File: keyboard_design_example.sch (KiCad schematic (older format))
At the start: 24 parts, among them SW1 SW_PUSH, U1 ATmega32U4-AU, Y1 16MHz

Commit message: Update and work
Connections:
- net +5V: no longer C1.2, C2.2, C3.2, C4.2, C5.2, C6.2, C7.2, R4.1, SW1.1, U1.15 (GND), U1.23 (GND), U1.35 (GND), U1.43 (GND), U1.5 (UGND), USB1.1 (GND), Y1.2, Y1.4
- new net GND: C1.2, C2.2, C3.2, C4.2, C5.2, C6.2, C7.2, R4.1, SW1.1, U1.15 (GND), U1.23 (GND), U1.35 (GND), U1.43 (GND), U1.5 (UGND), USB1.1 (GND), Y1.2, Y1.4
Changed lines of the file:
@@
 Wire Wire Line
 	5750 2100 5650 2100
-$Comp
-L keyboard_parts:GND #PWR0102
-U 1 1 60214B8A
-P 5400 5800
-F 0 "#PWR0102" H 5400 5850 20  0001 C CNN
-F 1 "GND" H 5400 5859 30  0000 C CNN
-F 2 "" H 5400 5800 60  0000 C CNN
-F 3 "" H 5400 5800 60  0000 C CNN
-	1    5400 5800
-	1    0    0    -1
-$EndComp
 Wire Wire Line
 	5750 5700 5650 5700
@@
 	0    1    1    0
 $EndComp
-$Comp
-L keyboard_parts:GND #PWR0103
-U 1 1 602192CF
-P 7500 4500
-F 0 "#PWR0103" H 7500 4550 20  0001 C CNN
-F 1 "GND" H 7500 4559 30  0000 C CNN
-F 2 "" H 7500 4500 60  0000 C CNN
-F 3 "" H 7500 4500 60  0000 C CNN
-	1    7500 4500
-	1    0    0    -1
-$EndComp
 Wire Wire Line
 	6350 4500 6900 4500
@@
 Wire Wire Line
 	4750 3700 4750 3850
-$Comp
-L keyboard_parts:GND #PWR0104
-U 1 1 6022339F
-P 4750 4250
-F 0 "#PWR0104" H 4750 4300 20  0001 C CNN
-F 1 "GND" H 4750 4309 30  0000 C CNN
-F 2 "" H 4750 4250 60  0000 C CNN
-F 3 "" H 4750 4250 60  0000 C CNN
-	1    4750 4250
-	1    0    0    -1
-$EndComp
 Wire Wire Line
 	4750 4050 4750 4250
@@
 Wire Wire Line
 	4250 3000 4100 3000
-$Comp
-L keyboard_parts:GND #PWR0106
-U 1 1 60232D3A
-P 4100 3100
-F 0 "#PWR0106" H 4100 3150 20  0001 C CNN
-F 1 "GND" H 4100 3159 30  0000 C CNN
-F 2 "" H 4100 3100 60  0000 C CNN
-F 3 "" H 4100 3100 60  0000 C CNN
-	1    4100 3100
-	1    0    0    -1
-$EndComp
 Wire Wire Line
 	4100 3000 4100 3100
@@
 Wire Wire Line
 	5150 2400 5100 2400
-$Comp
-L keyboard_parts:GND #PWR0107
-U 1 1 6023828E
-P 4400 2100
-F 0 "#PWR0107" H 4400 2150 20  0001 C CNN
-F 1 "GND" H 4400 2159 30  0000 C CNN
-F 2 "" H 4400 2100 60  0000 C CNN
-F 3 "" H 4400 2100 60  0000 C CNN
-	1    4400 2100
-	1    0    0    -1
-$EndComp
 $Comp
 L power:+5V #PWR0108
@@
 F 3 "" H 3600 4550 50  0001 C CNN
 	1    3600 4550
-	1    0    0    -1
-$EndComp
-$Comp
-L keyboard_parts:GND #PWR0110
-U 1 1 60244FF0
-P 3600 4950
-F 0 "#PWR0110" H 3600 5000 20  0001 C CNN
-F 1 "GND" H 3600 5009 30  0000 C CNN
-F 2 "" H 3600 4950 60  0000 C CNN
-F 3 "" H 3600 4950 60  0000 C CNN
-	1    3600 4950
 	1    0    0    -1
 $EndComp
@@
 Wire Wire Line
 	8450 2100 8450 2150
-$Comp
-L keyboard_parts:GND #PWR0113
-U 1 1 602538F7
-P 8450 2150
-F 0 "#PWR0113" H 8450 2200 20  0001 C CNN
-F 1 "GND" H 8450 2209 30  0000 C CNN
-F 2 "" H 8450 2150 60  0000 C CNN
-F 3 "" H 8450 2150 60  0000 C CNN
-	1    8450 2150
-	1    0    0    -1
-$EndComp
 Wire Wire Line
 	8300 1900 8500 1900
@@
 Wire Wire Line
 	4450 2100 4400 2100
+$Comp
+L power:GND #PWR0102
+U 1 1 60242F11
+P 3600 4950
+F 0 "#PWR0102" H 3600 4700 50  0001 C CNN
+F 1 "GND" H 3605 4777 50  0000 C CNN
+F 2 "" H 3600 4950 50  0001 C CNN
+F 3 "" H 3600 4950 50  0001 C CNN
+	1    3600 4950
+	1    0    0    -1
+$EndComp
+$Comp
+L power:GND #PWR0103
+U 1 1 60247D6C
+P 4100 3100
+F 0 "#PWR0103" H 4100 2850 50  0001 C CNN
+F 1 "GND" H 4105 2927 50  0000 C CNN
+F 2 "" H 4100 3100 50  0001 C CNN
+F 3 "" H 4100 3100 50  0001 C CNN
+	1    4100 3100
+	1    0    0    -1
+$EndComp
+$Comp
+L power:GND #PWR0104
+U 1 1 60249D69
+P 4400 2100
+F 0 "#PWR0104" H 4400 1850 50  0001 C CNN
+F 1 "GND" H 4405 1927 50  0000 C CNN
+F 2 "" H 4400 2100 50  0001 C CNN
+F 3 "" H 4400 2100 50  0001 C CNN
+	1    4400 2100
+	1    0    0    -1
+$EndComp
+$Comp
+L power:GND #PWR0106
+U 1 1 6024BCD7
+P 7500 4500
+F 0 "#PWR0106" H 7500 4250 50  0001 C CNN
+F 1 "GND" H 7505 4327 50  0000 C CNN
+F 2 "" H 7500 4500 50  0001 C CNN
+F 3 "" H 7500 4500 50  0001 C CNN
+	1    7500 4500
+	1    0    0    -1
+$EndComp
+$Comp
+L power:GND #PWR0107
+U 1 1 6024DB1C
+P 5400 5800
+F 0 "#PWR0107" H 5400 5550 50  0001 C CNN
+F 1 "GND" H 5405 5627 50  0000 C CNN
+F 2 "" H 5400 5800 50  0001 C CNN
+F 3 "" H 5400 5800 50  0001 C CNN
+	1    5400 5800
+	1    0    0    -1
+$EndComp
+$Comp
+L power:GND #PWR0110
+U 1 1 6024FA6D
+P 4750 4250
+F 0 "#PWR0110" H 4750 4000 50  0001 C CNN
+F 1 "GND" H 4755 4077 50  0000 C CNN
+F 2 "" H 4750 4250 50  0001 C CNN
+F 3 "" H 4750 4250 50  0001 C CNN
+	1    4750 4250
+	1    0    0    -1
+$EndComp
+$Comp
+L power:GND #PWR0113
+U 1 1 60251816
+P 8450 2150
+F 0 "#PWR0113" H 8450 1900 50  0001 C CNN
+F 1 "GND" H 8455 1977 50  0000 C CNN
+F 2 "" H 8450 2150 50  0001 C CNN
+F 3 "" H 8450 2150 50  0001 C CNN
+	1    8450 2150
+	1    0    0    -1
+$EndComp
 $EndSCHEMATC

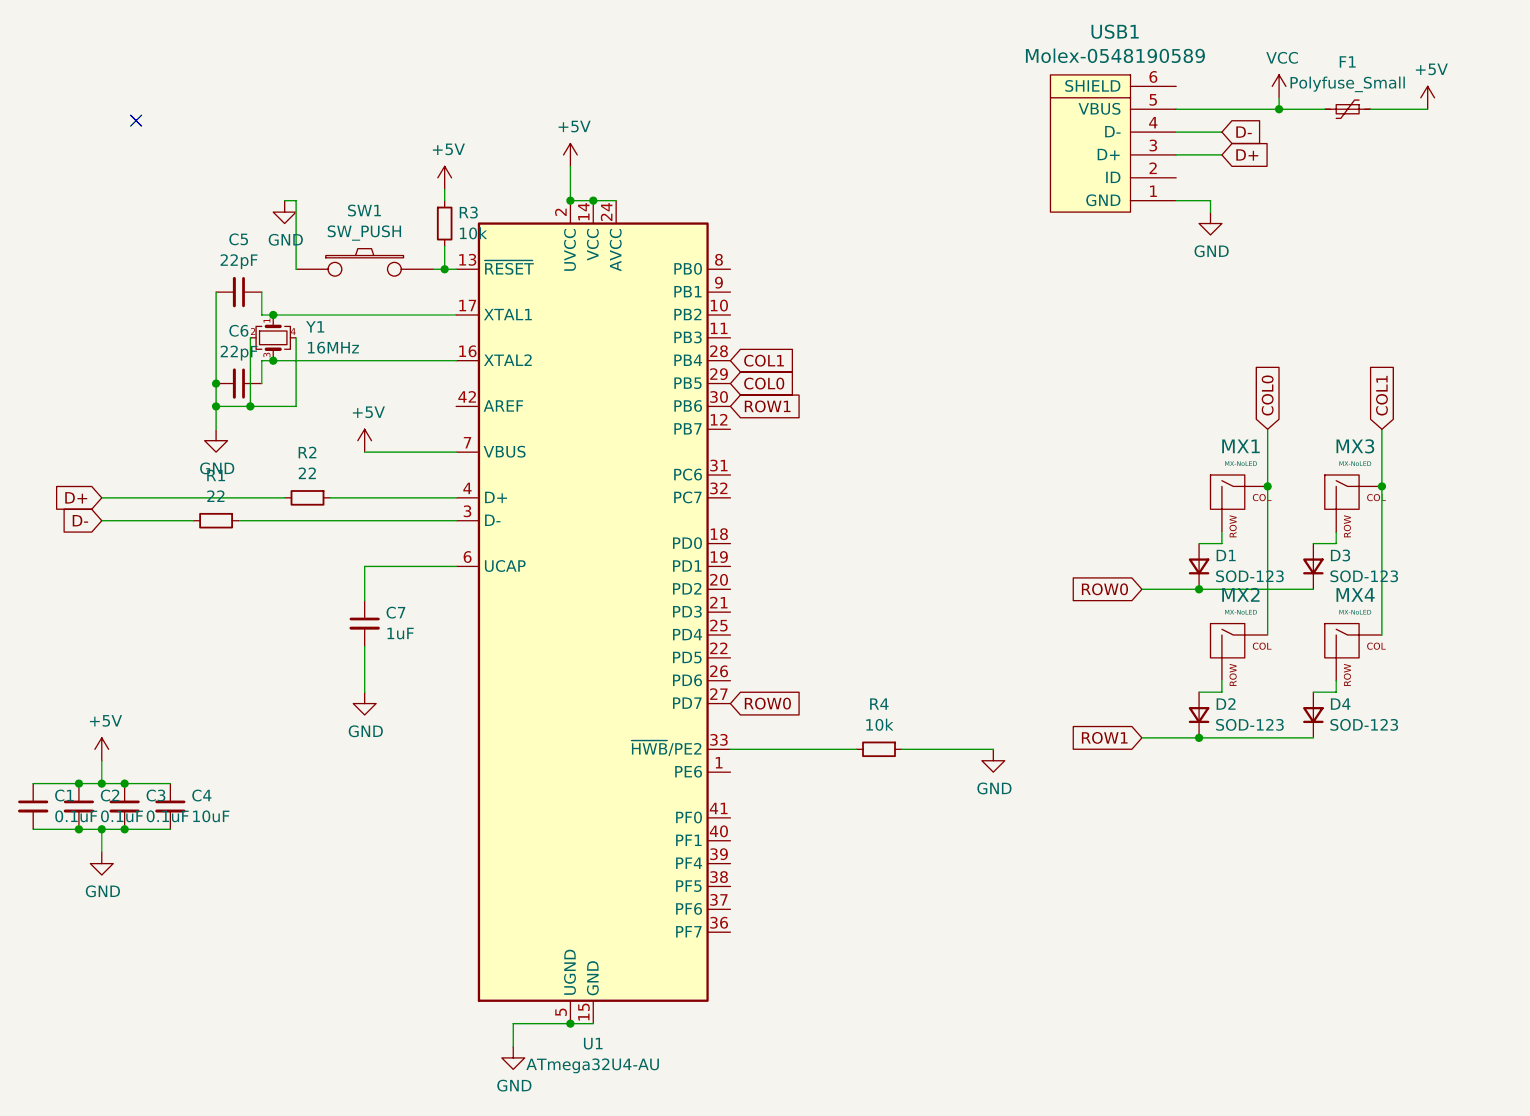
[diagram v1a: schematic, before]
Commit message: 2x2 bad 3x3 good
Updated schematic for a 3x3 mx switch cluster.
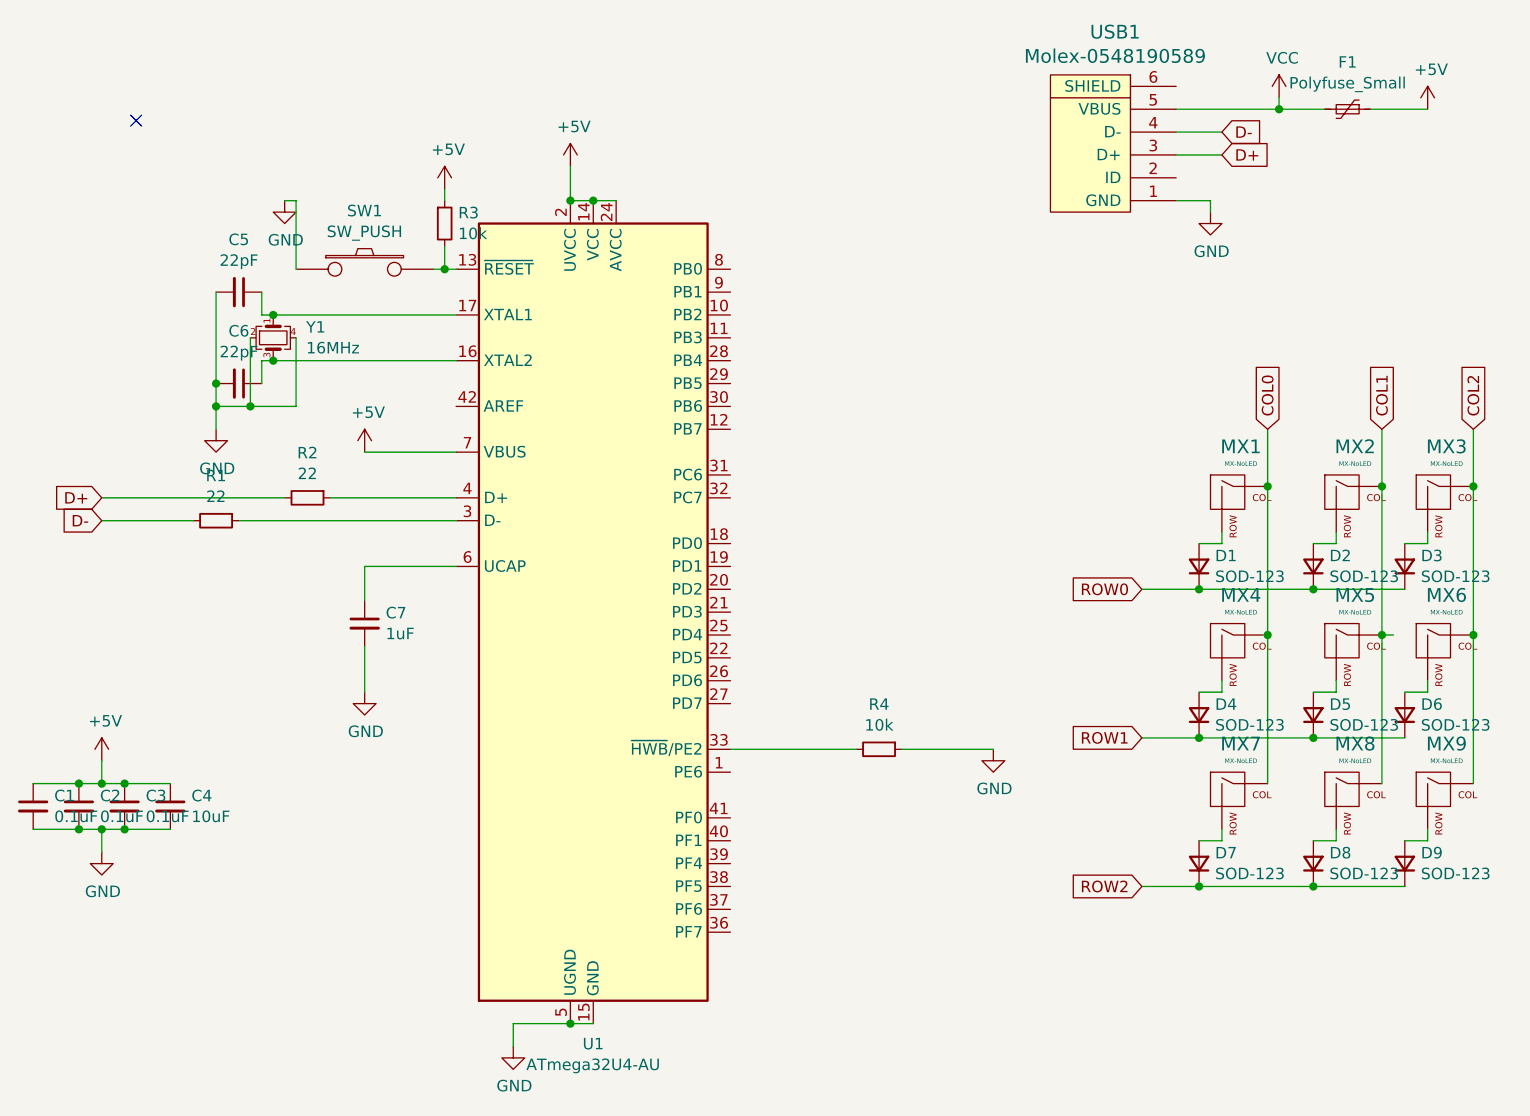
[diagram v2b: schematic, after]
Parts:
- added D3, D6, D7, D8, D9: SOD-123, symbol Device:D_Small
- added MX3, MX6, MX7, MX8, MX9: MX-NoLED, symbol MX_Alps_Hybrid:MX-NoLED
- renumbered D3 to D2, D2 to D4, D4 to D5, MX3 to MX2, MX2 to MX4, MX4 to MX5
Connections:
- net COL0: now also MX7.1 (COL); no longer U1.29 (PB5)
- net COL1: now also MX8.1 (COL); no longer U1.28 (PB4)
- net ROW0: now also D3.1 (K); no longer U1.27 (PD7)
- net ROW1: now also D6.1 (K); no longer U1.30 (PB6)
- new net: D3.2 (A), MX3.2 (ROW)
- new net: D6.2 (A), MX6.2 (ROW)
- new net: D8.2 (A), MX8.2 (ROW)
- new net: D9.2 (A), MX9.2 (ROW)
- new net: D7.2 (A), MX7.2 (ROW)
- new net COL2: MX3.1 (COL), MX6.1 (COL), MX9.1 (COL)
- new net ROW2: D7.1 (K), D8.1 (K), D9.1 (K)
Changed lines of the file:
@@
 	8500 3600 8400 3600
 $Comp
-L Device:D_Small D3
+L Device:D_Small D2
 U 1 1 60269C14
 P 8900 3700
-F 0 "D3" V 8946 3630 50  0000 R CNN
+F 0 "D2" V 8946 3630 50  0000 R CNN
 F 1 "SOD-123" V 8855 3630 50  0000 R CNN
 F 2 "Diode_SMD:D_SOD-123" V 8900 3700 50  0001 C CNN
@@
 $EndComp
 $Comp
-L MX_Alps_Hybrid:MX-NoLED MX2
+L MX_Alps_Hybrid:MX-NoLED MX4
 U 1 1 60270EEF
 P 8550 4050
-F 0 "MX2" H 8583 4273 60  0000 C CNN
+F 0 "MX4" H 8583 4273 60  0000 C CNN
 F 1 "MX-NoLED" H 8583 4199 20  0000 C CNN
 F 2 "MX_Only:MXOnly-1U-NoLED" H 7925 4025 60  0001 C CNN
@@
 $EndComp
 $Comp
-L Device:D_Small D2
+L Device:D_Small D4
 U 1 1 60270EF5
 P 8400 4350
-F 0 "D2" V 8446 4280 50  0000 R CNN
+F 0 "D4" V 8446 4280 50  0000 R CNN
 F 1 "SOD-123" V 8355 4280 50  0000 R CNN
 F 2 "Diode_SMD:D_SOD-123" V 8400 4350 50  0001 C CNN
@@
 	8500 4250 8400 4250
 $Comp
-L MX_Alps_Hybrid:MX-NoLED MX3
+L MX_Alps_Hybrid:MX-NoLED MX2
 U 1 1 60269C0E
 P 9050 3400
-F 0 "MX3" H 9083 3623 60  0000 C CNN
+F 0 "MX2" H 9083 3623 60  0000 C CNN
 F 1 "MX-NoLED" H 9083 3549 20  0000 C CNN
 F 2 "MX_Only:MXOnly-1U-NoLED" H 8425 3375 60  0001 C CNN
@@
 	9000 3550 9000 3600
 $Comp
-L MX_Alps_Hybrid:MX-NoLED MX4
+L MX_Alps_Hybrid:MX-NoLED MX5
 U 1 1 6027F391
 P 9050 4050
-F 0 "MX4" H 9083 4273 60  0000 C CNN
+F 0 "MX5" H 9083 4273 60  0000 C CNN
 F 1 "MX-NoLED" H 9083 4199 20  0000 C CNN
 F 2 "MX_Only:MXOnly-1U-NoLED" H 8425 4025 60  0001 C CNN
@@
 $EndComp
 $Comp
-L Device:D_Small D4
+L Device:D_Small D5
 U 1 1 6027F397
 P 8900 4350
-F 0 "D4" V 8946 4280 50  0000 R CNN
+F 0 "D5" V 8946 4280 50  0000 R CNN
 F 1 "SOD-123" V 8855 4280 50  0000 R CNN
 F 2 "Diode_SMD:D_SOD-123" V 8900 4350 50  0001 C CNN
@@
 Text GLabel 9200 3100 1    50   Input ~ 0
 COL1
-Text GLabel 6350 2800 2    50   Input ~ 0
-COL1
-Text GLabel 6350 2900 2    50   Input ~ 0
-COL0
-Text GLabel 6350 3000 2    50   Input ~ 0
-ROW1
-Text GLabel 6350 4300 2    50   Input ~ 0
-ROW0
 Wire Wire Line
 	5100 2400 5050 2400
@@
 	1    0    0    -1
 $EndComp
+$Comp
+L MX_Alps_Hybrid:MX-NoLED MX3
+U 1 1 602AE95C
+P 9450 3400
+F 0 "MX3" H 9483 3623 60  0000 C CNN
+F 1 "MX-NoLED" H 9483 3549 20  0000 C CNN
+F 2 "" H 8825 3375 60  0001 C CNN
+F 3 "" H 8825 3375 60  0001 C CNN
+	1    9450 3400
+	1    0    0    -1
+$EndComp
+$Comp
+L MX_Alps_Hybrid:MX-NoLED MX6
+U 1 1 602B0C61
+P 9450 4050
+F 0 "MX6" H 9483 4273 60  0000 C CNN
+F 1 "MX-NoLED" H 9483 4199 20  0000 C CNN
+F 2 "" H 8825 4025 60  0001 C CNN
+F 3 "" H 8825 4025 60  0001 C CNN
+	1    9450 4050
+	1    0    0    -1
+$EndComp
+$Comp
+L MX_Alps_Hybrid:MX-NoLED MX8
+U 1 1 602B2612
+P 9050 4700
+F 0 "MX8" H 9083 4923 60  0000 C CNN
+F 1 "MX-NoLED" H 9083 4849 20  0000 C CNN
+F 2 "" H 8425 4675 60  0001 C CNN
+F 3 "" H 8425 4675 60  0001 C CNN
+	1    9050 4700
+	1    0    0    -1
+$EndComp
+$Comp
+L MX_Alps_Hybrid:MX-NoLED MX9
+U 1 1 602B3220
+P 9450 4700
+F 0 "MX9" H 9483 4923 60  0000 C CNN
+F 1 "MX-NoLED" H 9483 4849 20  0000 C CNN
+F 2 "" H 8825 4675 60  0001 C CNN
+F 3 "" H 8825 4675 60  0001 C CNN
+	1    9450 4700
+	1    0    0    -1
+$EndComp
+$Comp
+L MX_Alps_Hybrid:MX-NoLED MX7
+U 1 1 602B59E8
+P 8550 4700
+F 0 "MX7" H 8583 4923 60  0000 C CNN
+F 1 "MX-NoLED" H 8583 4849 20  0000 C CNN
+F 2 "" H 7925 4675 60  0001 C CNN
+F 3 "" H 7925 4675 60  0001 C CNN
+	1    8550 4700
+	1    0    0    -1
+$EndComp
+Wire Wire Line
+	8700 4650 8700 4000
+Connection ~ 8700 4000
+Wire Wire Line
+	9200 4650 9200 4000
+Wire Wire Line
+	9200 4000 9250 4000
+Connection ~ 9200 4000
+Wire Wire Line
+	9600 3100 9600 3350
+Connection ~ 9600 3350
+Wire Wire Line
+	9600 3350 9600 4000
+Connection ~ 9600 4000
+Wire Wire Line
+	9600 4000 9600 4650
+Wire Wire Line
+	9400 4200 9400 4250
+Wire Wire Line
+	9400 4250 9300 4250
+$Comp
+L Device:D_Small D6
+U 1 1 602C077F
+P 9300 4350
+F 0 "D6" V 9346 4280 50  0000 R CNN
+F 1 "SOD-123" V 9255 4280 50  0000 R CNN
+F 2 "" V 9300 4350 50  0001 C CNN
+F 3 "~" V 9300 4350 50  0001 C CNN
+	1    9300 4350
+	0    -1   -1   0
+$EndComp
+Wire Wire Line
+	9300 4450 8900 4450
+Connection ~ 8900 4450
+$Comp
+L Device:D_Small D9
+U 1 1 602D2010
+P 9300 5000
+F 0 "D9" V 9346 4930 50  0000 R CNN
+F 1 "SOD-123" V 9255 4930 50  0000 R CNN
+F 2 "" V 9300 5000 50  0001 C CNN
+F 3 "~" V 9300 5000 50  0001 C CNN
+	1    9300 5000
+	0    -1   -1   0
+$EndComp
+$Comp
+L Device:D_Small D8
+U 1 1 602D3109
+P 8900 5000
+F 0 "D8" V 8946 4930 50  0000 R CNN
+F 1 "SOD-123" V 8855 4930 50  0000 R CNN
+F 2 "" V 8900 5000 50  0001 C CNN
+F 3 "~" V 8900 5000 50  0001 C CNN
+	1    8900 5000
+	0    -1   -1   0
+$EndComp
+$Comp
+L Device:D_Small D7
+U 1 1 602D3623
+P 8400 5000
+F 0 "D7" V 8446 4930 50  0000 R CNN
+F 1 "SOD-123" V 8355 4930 50  0000 R CNN
+F 2 "" V 8400 5000 50  0001 C CNN
+F 3 "~" V 8400 5000 50  0001 C CNN
+	1    8400 5000
+	0    -1   -1   0
+$EndComp
+Wire Wire Line
+	8500 4850 8500 4900
+Wire Wire Line
+	8500 4900 8400 4900
+Wire Wire Line
+	9000 4850 9000 4900
+Wire Wire Line
+	9000 4900 8900 4900
+Wire Wire Line
+	9400 4850 9400 4900
+Wire Wire Line
+	9400 4900 9300 4900
+Wire Wire Line
+	9300 5100 8900 5100
+Connection ~ 8400 5100
+Wire Wire Line
+	8400 5100 8150 5100
+Connection ~ 8900 5100
+Wire Wire Line
+	8900 5100 8400 5100
+Wire Wire Line
+	8900 3800 9300 3800
+Connection ~ 8900 3800
+$Comp
+L Device:D_Small D3
+U 1 1 602DEC6E
+P 9300 3700
+F 0 "D3" V 9346 3630 50  0000 R CNN
+F 1 "SOD-123" V 9255 3630 50  0000 R CNN
+F 2 "" V 9300 3700 50  0001 C CNN
+F 3 "~" V 9300 3700 50  0001 C CNN
+	1    9300 3700
+	0    -1   -1   0
+$EndComp
+Wire Wire Line
+	9400 3550 9400 3600
+Wire Wire Line
+	9400 3600 9300 3600
+Text GLabel 8150 5100 0    50   Input ~ 0
+ROW2
+Text GLabel 9600 3100 1    50   Input ~ 0
+COL2
 $EndSCHEMATC

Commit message: Update
Working on pcb organization
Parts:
- D3, D6, D7, D8, D9: footprint (none) -> Diode_SMD:D_SOD-123
- MX3, MX6, MX7, MX8, MX9: footprint (none) -> MX_Only:MXOnly-1U-NoLED
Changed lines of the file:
@@
 F 0 "MX3" H 9483 3623 60  0000 C CNN
 F 1 "MX-NoLED" H 9483 3549 20  0000 C CNN
-F 2 "" H 8825 3375 60  0001 C CNN
+F 2 "MX_Only:MXOnly-1U-NoLED" H 8825 3375 60  0001 C CNN
 F 3 "" H 8825 3375 60  0001 C CNN
 	1    9450 3400
@@
 F 0 "MX6" H 9483 4273 60  0000 C CNN
 F 1 "MX-NoLED" H 9483 4199 20  0000 C CNN
-F 2 "" H 8825 4025 60  0001 C CNN
+F 2 "MX_Only:MXOnly-1U-NoLED" H 8825 4025 60  0001 C CNN
 F 3 "" H 8825 4025 60  0001 C CNN
 	1    9450 4050
@@
 F 0 "MX8" H 9083 4923 60  0000 C CNN
 F 1 "MX-NoLED" H 9083 4849 20  0000 C CNN
-F 2 "" H 8425 4675 60  0001 C CNN
+F 2 "MX_Only:MXOnly-1U-NoLED" H 8425 4675 60  0001 C CNN
 F 3 "" H 8425 4675 60  0001 C CNN
 	1    9050 4700
@@
 F 0 "MX9" H 9483 4923 60  0000 C CNN
 F 1 "MX-NoLED" H 9483 4849 20  0000 C CNN
-F 2 "" H 8825 4675 60  0001 C CNN
+F 2 "MX_Only:MXOnly-1U-NoLED" H 8825 4675 60  0001 C CNN
 F 3 "" H 8825 4675 60  0001 C CNN
 	1    9450 4700
@@
 F 0 "MX7" H 8583 4923 60  0000 C CNN
 F 1 "MX-NoLED" H 8583 4849 20  0000 C CNN
-F 2 "" H 7925 4675 60  0001 C CNN
+F 2 "MX_Only:MXOnly-1U-NoLED" H 7925 4675 60  0001 C CNN
 F 3 "" H 7925 4675 60  0001 C CNN
 	1    8550 4700
@@
 F 0 "D6" V 9346 4280 50  0000 R CNN
 F 1 "SOD-123" V 9255 4280 50  0000 R CNN
-F 2 "" V 9300 4350 50  0001 C CNN
+F 2 "Diode_SMD:D_SOD-123" V 9300 4350 50  0001 C CNN
 F 3 "~" V 9300 4350 50  0001 C CNN
 	1    9300 4350
@@
 F 0 "D9" V 9346 4930 50  0000 R CNN
 F 1 "SOD-123" V 9255 4930 50  0000 R CNN
-F 2 "" V 9300 5000 50  0001 C CNN
+F 2 "Diode_SMD:D_SOD-123" V 9300 5000 50  0001 C CNN
 F 3 "~" V 9300 5000 50  0001 C CNN
 	1    9300 5000
@@
 F 0 "D8" V 8946 4930 50  0000 R CNN
 F 1 "SOD-123" V 8855 4930 50  0000 R CNN
-F 2 "" V 8900 5000 50  0001 C CNN
+F 2 "Diode_SMD:D_SOD-123" V 8900 5000 50  0001 C CNN
 F 3 "~" V 8900 5000 50  0001 C CNN
 	1    8900 5000
@@
 F 0 "D7" V 8446 4930 50  0000 R CNN
 F 1 "SOD-123" V 8355 4930 50  0000 R CNN
-F 2 "" V 8400 5000 50  0001 C CNN
+F 2 "Diode_SMD:D_SOD-123" V 8400 5000 50  0001 C CNN
 F 3 "~" V 8400 5000 50  0001 C CNN
 	1    8400 5000
@@
 F 0 "D3" V 9346 3630 50  0000 R CNN
 F 1 "SOD-123" V 9255 3630 50  0000 R CNN
-F 2 "" V 9300 3700 50  0001 C CNN
+F 2 "Diode_SMD:D_SOD-123" V 9300 3700 50  0001 C CNN
 F 3 "~" V 9300 3700 50  0001 C CNN
 	1    9300 3700

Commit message: Finished
WOOOO I think i finished. Might have to do some updates for fixes but its going good.
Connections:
- net COL0: now also U1.27 (PD7)
- net COL1: now also U1.28 (PB4)
- net COL2: now also U1.30 (PB6)
- net ROW0: now also U1.29 (PB5)
- net ROW1: now also U1.31 (PC6)
- net ROW2: now also U1.32 (PC7)
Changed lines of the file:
@@
 Text GLabel 9600 3100 1    50   Input ~ 0
 COL2
+Text GLabel 6350 3400 2    50   Input ~ 0
+ROW2
+Text GLabel 6350 3300 2    50   Input ~ 0
+ROW1
+Text GLabel 6350 2900 2    50   Input ~ 0
+ROW0
+Text GLabel 6350 3000 2    50   Input ~ 0
+COL2
+Text GLabel 6350 2800 2    50   Input ~ 0
+COL1
+Text GLabel 6350 4300 2    50   Input ~ 0
+COL0
 $EndSCHEMATC
